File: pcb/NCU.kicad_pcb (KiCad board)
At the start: 4 copper layers, 100 x 150 mm, 332 parts, among them IC1 VND7E025AJTR, IC2 ESP32-C6-WROOM-1-N8, IC3 ESD2CAN24DBZRQ1, IC4 VND7E025AJTR, IC5 ESD2CAN24DBZRQ1, IC6 LMR51460SQDRRRQ1, IC7 TPS628101HQWRWYRQ1, IC8 LP2951-50DRG4, IC9 TPS2121RUXT, J1 6437288-4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

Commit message: initial microcontroller layout
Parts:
- JP6, JP7, JP8: moved to B.Cu
- L1: value VLS3015CX-2R2M-H -> 2.2uH; footprint SamacSys_Parts:VLS3015 -> Inductor_SMD:L_0805_2012Metric_Pad1.05x1.20mm_HandSolder
- moved D27 322.6 mm to (145.4, 127.0)
- moved D26 322.2 mm to (140.7, 155.9)
- moved U7 313.1 mm to (130.9, 137.3)
- moved TP18 313.1 mm to (125.6, 116.9), turned to 90 degrees
- moved R124 311.5 mm to (140.7, 154.4)
- moved JP12 296.9 mm to (125.0, 119.8), turned to 180 degrees
- moved TP19 295.8 mm to (105.7, 141.3)
- moved Y2 292.7 mm to (108.5, 133.3), turned to 90 degrees
- moved R125 289.5 mm to (125.0, 121.8), turned to 180 degrees
- moved Y3 287.7 mm to (112.4, 146.6)
- moved C90 284.7 mm to (112.3, 144.4), turned to 180 degrees
- moved C92 284.6 mm to (112.3, 149.2)
- moved R126 284.3 mm to (120.1, 121.8)
- moved C89 281.6 mm to (109.6, 140.4), turned to 90 degrees
- moved C17 279.7 mm to (147.1, 134.6), turned to 90 degrees
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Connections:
- C91 pad 1: /MCU/RCC_OSC_OUT -> /MCU/RCC_OSC32_OUT
- C93 pad 1: /MCU/RCC_OSC_IN -> /MCU/RCC_OSC32_IN
- Y2 pad 1: /MCU/RCC_OSC_OUT -> /MCU/RCC_OSC32_OUT
- Y2 pad 2: /MCU/RCC_OSC_IN -> /MCU/RCC_OSC32_IN
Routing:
- net 3V3: track 10.4 -> 130.9 mm, vias 10 -> 30
- net /MCU/MCU Power/VDDLDO: track 0.00 -> 77.3 mm, vias 0 -> 3
- net /MCU/VCAP: track 0.00 -> 73.0 mm, vias 0 -> 3
- net GND: track 14.0 -> 77.3 mm, vias 53 -> 101
- net /MCU/RCC_OSC_IN: track 0.00 -> 20.4 mm
- net /MCU/STM_NRST: track 0.00 -> 15.7 mm, vias 0 -> 2
- net /MCU/MCU Power/1V2_MCU: track 0.00 -> 14.9 mm, vias 0 -> 1
- net /MCU/RCC_OSC32_OUT: track 0.00 -> 14.5 mm
- net /MCU/RCC_OSC32_IN: track 0.00 -> 14.4 mm
- net Net-(JP12-A): track 0.00 -> 11.1 mm
- net /MCU/RCC_OSC_OUT: track 0.00 -> 11.1 mm
- net Net-(U7-PE15): track 0.00 -> 8.41 mm
- net /MCU/MCU Power/VDDA: track 0.00 -> 8.27 mm, vias 0 -> 1
- net /MCU/VREF+: track 0.00 -> 7.61 mm, vias 0 -> 1
- net /MCU/VFBSMPS: track 0.00 -> 7.45 mm, vias 0 -> 1
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- added copper zone on In2.Cu, net 3V3

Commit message: laid out analogs
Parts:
- JP11: moved to B.Cu
- moved TP14 356.3 mm to (181.8, 96.6), turned to 90 degrees
- moved TP15 356.1 mm to (181.8, 103.6), turned to 90 degrees
- moved R85 350.3 mm to (183.5, 100.1), turned to -90 degrees
- moved IC3 347.0 mm to (180.7, 100.1), turned to 180 degrees
- moved U4 343.1 mm to (174.9, 100.0)
- moved C67 341.2 mm to (170.4, 100.1), turned to 90 degrees
- moved C66 339.5 mm to (168.8, 100.1), turned to 90 degrees
- moved TP17 330.7 mm to (181.7, 91.7), turned to 90 degrees
- moved TP16 330.2 mm to (181.7, 84.7), turned to 90 degrees
- moved R109 323.0 mm to (183.5, 88.2), turned to -90 degrees
- moved IC5 320.4 mm to (180.7, 88.2), turned to 180 degrees
- moved U5 317.6 mm to (174.9, 88.2)
- moved C72 314.3 mm to (170.3, 88.0), turned to 90 degrees
- moved C71 313.0 mm to (168.7, 88.0), turned to 90 degrees
- moved D10 257.5 mm to (86.7, 124.2)
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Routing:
- net AGND: track 17.7 -> 73.9 mm, vias 5 -> 40
- net 3V3: track 130.9 -> 157.9 mm, vias 30 -> 45
- net GND: track 77.3 -> 90.0 mm, vias 101 -> 111
- net /CONN_A/CAN0_L: track 0.00 -> 8.83 mm
- net /CONN_A/CAN0_H: track 0.00 -> 8.80 mm
- net /CONN_A/CAN1_L: track 0.00 -> 8.79 mm
- net /CONN_A/CAN1_H: track 0.00 -> 8.75 mm
- net /INPUTS/DIN2_IO: track 0.00 -> 3.74 mm
- net /GPIO/GPIO1_IO: track 0.00 -> 3.73 mm
- net /GPIO/GPIO2_IO: track 0.00 -> 3.72 mm
- net /GPIO/GPIO3_IO: track 0.00 -> 3.72 mm
- net /INPUTS/AIN0_IO: track 0.00 -> 3.71 mm
- net /INPUTS/AIN2_IO: track 0.00 -> 3.71 mm
- net /INPUTS/12V_IO: track 0.00 -> 3.70 mm
- net /INPUTS/DIN1_IO: track 0.00 -> 3.70 mm
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
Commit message: v2 analogs routing
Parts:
- moved D14 343.8 mm to (145.8, 114.8), turned to 180 degrees
- moved R49 340.6 mm to (143.2, 111.9), turned to 0 degrees
- moved C50 339.8 mm to (143.2, 113.4), turned to 180 degrees
- moved D6 334.9 mm to (145.9, 119.3), turned to 180 degrees
- moved D18 334.6 mm to (135.0, 113.8), turned to 180 degrees
- moved R47 334.2 mm to (139.9, 111.9), turned to 0 degrees
- moved R48 333.3 mm to (139.8, 113.4), turned to 180 degrees
- moved R19 331.5 mm to (143.2, 116.4), turned to 0 degrees
- moved R67 331.5 mm to (132.3, 110.9), turned to 0 degrees
- moved C12 330.8 mm to (143.2, 117.9), turned to 180 degrees
- moved C56 330.6 mm to (132.3, 112.4), turned to 180 degrees
- moved D11 325.9 mm to (145.8, 123.9), turned to 180 degrees
- moved D16 325.5 mm to (135.0, 118.3), turned to 180 degrees
- moved R63 325.3 mm to (129.0, 110.9), turned to 0 degrees
- moved R17 325.2 mm to (139.9, 116.4), turned to 0 degrees
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
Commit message: routed LSDs
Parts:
- moved R86 356.1 mm to (212.4, 135.3), turned to 180 degrees
- moved R87 355.8 mm to (212.4, 136.9), turned to 180 degrees
- moved S2 355.2 mm to (217.9, 137.2)
- moved R89 354.9 mm to (212.4, 138.5)
- moved R20 354.6 mm to (212.4, 141.7), turned to 180 degrees
- moved R21 354.3 mm to (212.4, 143.3), turned to 180 degrees
- moved R88 354.3 mm to (212.4, 133.7), turned to 180 degrees
- moved S1 353.7 mm to (217.9, 143.7)
- moved R23 353.5 mm to (212.4, 144.9)
- moved R22 352.9 mm to (212.4, 140.1), turned to 180 degrees
- moved R104 347.7 mm to (212.4, 154.5), turned to 180 degrees
- moved R105 347.4 mm to (212.4, 156.1), turned to 180 degrees
- moved S4 346.8 mm to (217.9, 156.4)
- moved R107 346.3 mm to (212.4, 157.7)
- moved R106 345.6 mm to (212.4, 152.9), turned to 180 degrees
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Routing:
- net 3V3: track 157.9 -> 215.0 mm, vias 45 -> 49
- net /MCU/MCU Power/VDDLDO: track 77.3 -> 24.4 mm
- net GND: track 90.0 -> 94.3 mm, vias 111 -> 139
- net Net-(S2-STATUS): track 0.00 -> 4.24 mm
- net Net-(S1-STATUS): track 0.00 -> 4.23 mm
- net Net-(S3-STATUS): track 0.00 -> 4.17 mm
- net Net-(S4-STATUS): track 0.00 -> 4.16 mm
- net Net-(S1-IN): track 0.00 -> 3.51 mm
- net Net-(S2-IN): track 0.00 -> 3.49 mm
- net Net-(S3-IN): track 0.00 -> 3.49 mm
- net Net-(S4-IN): track 0.00 -> 3.48 mm

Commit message: initial hsd layout
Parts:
- D23, D7: value 1N4148 -> 1N4148W; footprint Diode_THT:D_DO-35_SOD27_P7.62mm_Horizontal -> Diode_SMD:D_SOD-123
- moved R104 126.0 mm to (93.2, 113.6)
- moved R106 126.0 mm to (93.2, 112.0)
- moved R21 126.0 mm to (93.2, 102.4)
- moved R23 126.0 mm to (93.2, 104.0)
- moved R86 126.0 mm to (93.2, 94.4)
- moved R89 126.0 mm to (93.2, 97.6)
- moved R92 126.0 mm to (93.2, 105.6)
- moved S1 126.0 mm to (98.7, 102.8)
- moved S2 126.0 mm to (98.7, 96.3)
- moved S4 126.0 mm to (98.7, 115.5)
- moved R87 126.0 mm to (93.2, 96.0)
- moved R93 126.0 mm to (93.2, 110.4)
- moved R105 126.0 mm to (93.2, 115.2)
- moved R107 126.0 mm to (93.2, 116.8)
- moved R22 126.0 mm to (93.2, 99.2)
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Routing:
- net GND: track 94.3 -> 108.2 mm, vias 139 -> 153
- net Net-(IC4-~{FAULTRST}): track 0.00 -> 8.07 mm
- net Net-(IC1-~{FAULTRST}): track 0.00 -> 7.88 mm
- net Net-(IC1-CS): track 0.00 -> 7.40 mm
- net Net-(IC4-CS): track 0.00 -> 7.40 mm
- net Net-(IC4-SEN): track 0.00 -> 7.07 mm
- net Net-(D7-A): track 0.00 -> 6.91 mm
- net Net-(D23-A): track 0.00 -> 6.89 mm
- net Net-(IC1-SEN): track 0.00 -> 6.88 mm
- net Net-(IC1-SEL0): track 0.00 -> 5.69 mm
- net Net-(IC4-SEL0): track 0.00 -> 5.68 mm
- net Net-(IC1-INPUT0): track 0.00 -> 3.37 mm
- net Net-(IC4-INPUT0): track 0.00 -> 3.33 mm
- net Net-(IC4-INPUT1): track 0.00 -> 3.33 mm
- net Net-(IC1-INPUT1): track 0.00 -> 3.31 mm
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- added copper zone on F.Cu, net /CONN_A/HSD_0
- added copper zone on F.Cu, net /CONN_A/HSD_1
- added copper zone on F.Cu, net /CONN_A/HSD_2
- added copper zone on F.Cu, net /CONN_A/HSD_3

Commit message: improved power supplies I think
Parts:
- moved D14 294.5 mm to (-14.6, -31.6), turned to -90 degrees
- moved D6 293.0 mm to (-10.1, -31.6), turned to -90 degrees
- moved R49 292.0 mm to (-17.5, -28.9), turned to 90 degrees
- moved D11 291.5 mm to (-5.52, -31.6), turned to -90 degrees
- moved C50 291.4 mm to (-16.0, -28.9), turned to -90 degrees
- moved R19 290.3 mm to (-13.0, -28.9), turned to 90 degrees
- moved D15 290.2 mm to (-1.07, -31.6), turned to -90 degrees
- moved C12 289.8 mm to (-11.5, -28.9), turned to -90 degrees
- moved R42 288.8 mm to (-8.47, -28.9), turned to 90 degrees
- moved C48 288.3 mm to (-6.97, -28.9), turned to -90 degrees
- moved R47 287.5 mm to (-17.5, -25.6), turned to 90 degrees
- moved R52 287.4 mm to (-3.97, -29.0), turned to 90 degrees
- moved C51 286.9 mm to (-2.47, -29.0), turned to -90 degrees
- moved R48 286.8 mm to (-16.0, -25.6), turned to -90 degrees
- moved R17 285.8 mm to (-13.0, -25.6), turned to 90 degrees
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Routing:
- net Net-(IC9-CP2): track 5.80 -> 14.2 mm
- net Net-(IC9-PR1): track 4.45 -> 10.1 mm
- net GND: track 108.2 -> 107.2 mm, vias 153 -> 156
- net 5V: vias 3 -> 21

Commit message: improved power input stage, possible drive placement
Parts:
- moved C81 192.4 mm to (-13.8, 57.3)
- moved IC7 192.4 mm to (-13.8, 60.4)
- moved R114 192.4 mm to (-17.3, 61.3)
- moved TP9 192.4 mm to (-18.5, 68.9)
- moved C80 192.4 mm to (-9.38, 60.6)
- moved C82 192.4 mm to (-9.38, 63.8)
- moved C83 192.4 mm to (-14.5, 68.7)
- moved C84 192.4 mm to (-14.5, 71.2)
- moved C85 192.4 mm to (-14.5, 73.2)
- moved C86 192.4 mm to (-7.60, 25.9)
- moved C87 192.4 mm to (-17.7, 27.9)
- moved IC8 192.4 mm to (-13.1, 27.9)
- moved L3 192.4 mm to (-15.0, 65.3)
- moved R115 192.4 mm to (-9.38, 59.0)
- moved R116 192.4 mm to (-9.38, 65.4)
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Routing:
- net LV_5V: vias 15 -> 30
- net 12V: vias 0 -> 24
- net /PWR/PWR_LV_5V/LMR_SW: vias 0 -> 8

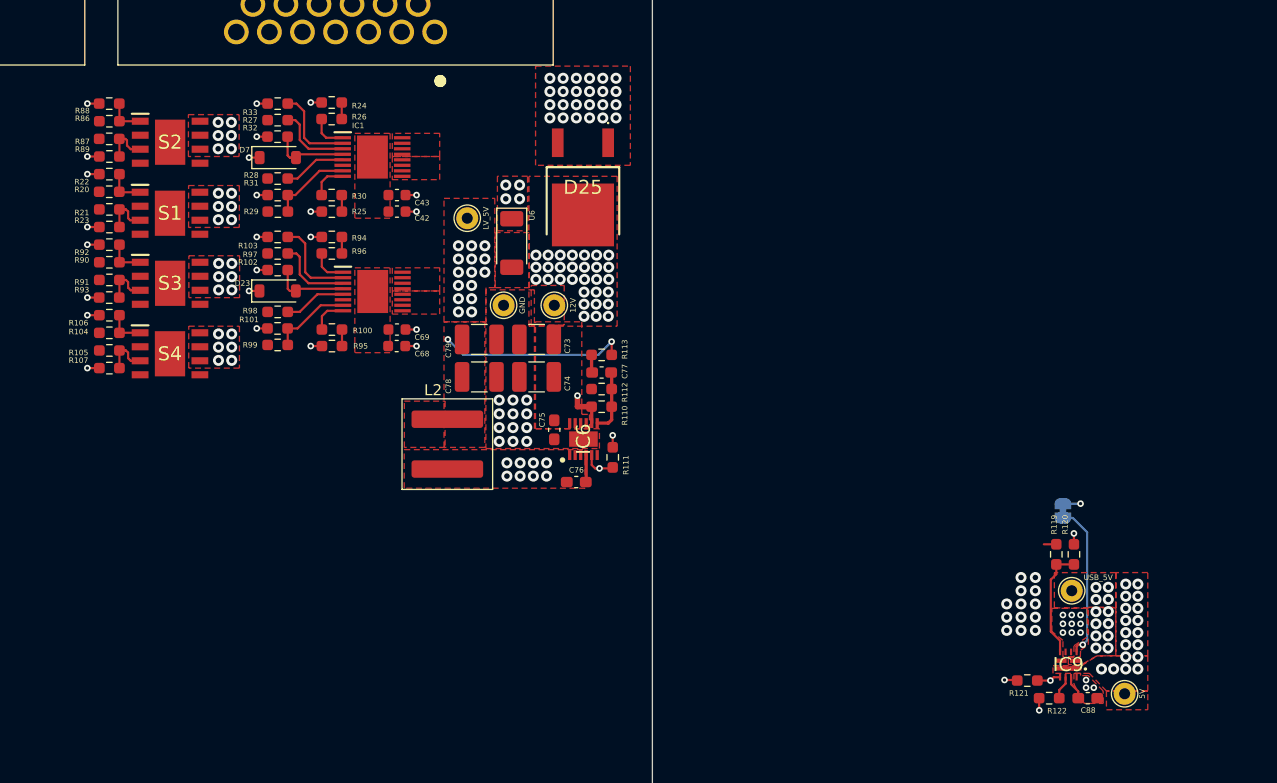
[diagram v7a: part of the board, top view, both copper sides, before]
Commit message: better power mux layout
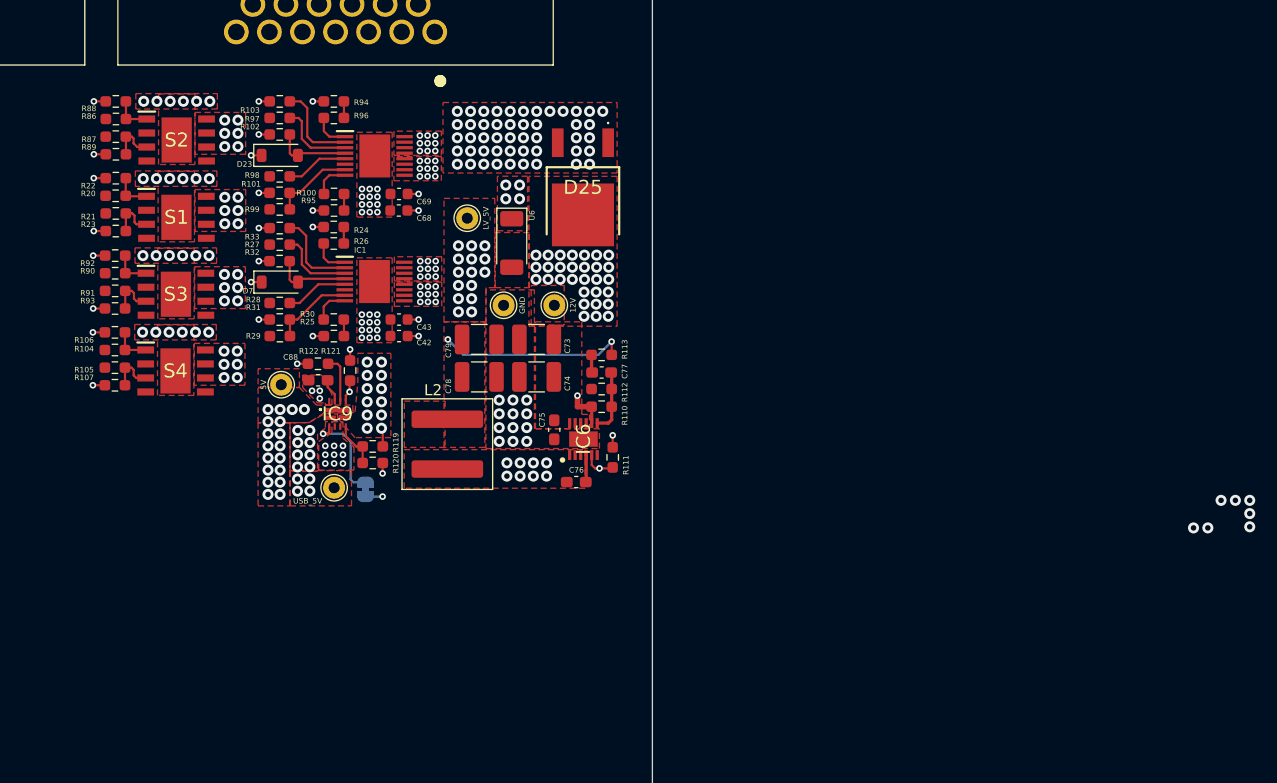
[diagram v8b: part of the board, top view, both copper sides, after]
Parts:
- moved TP8 81.5 mm to (116.3, 101.0), turned to 0 degrees
- moved C88 75.6 mm to (119.7, 100.6), turned to 180 degrees
- moved R122 73.0 mm to (119.7, 99.1)
- moved IC9 70.1 mm to (121.4, 103.7), turned to 0 degrees
- moved R121 67.6 mm to (122.6, 99.7), turned to -90 degrees
- moved TP6 67.6 mm to (121.1, 110.4), turned to -90 degrees
- moved R120 64.2 mm to (124.6, 108.1), turned to 0 degrees
- moved JP11 63.3 mm to (124.0, 110.5), turned to -90 degrees
- moved R119 62.8 mm to (124.6, 106.6), turned to 180 degrees
- moved R101 12.3 mm to (116.2, 83.6)
- moved R98 12.3 mm to (116.2, 82.1)
- moved R99 12.3 mm to (116.2, 85.1)
- moved C68 12.3 mm to (127.0, 85.2)
- moved C69 12.3 mm to (127.0, 83.7)
- moved D23 12.3 mm to (116.2, 80.2)
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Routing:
- net 3V3: track 217.0 -> 164.0 mm
- net USB_VBUS: track 0.00 -> 52.8 mm
- net 5V: track 11.0 -> 56.2 mm
- net /MCU/VCAP: track 73.0 -> 27.8 mm
- net Net-(IC9-PR1): track 10.1 -> 4.28 mm
- net Net-(IC9-CP2): track 14.2 -> 8.81 mm
- net Net-(IC9-ILIM): track 2.14 -> 4.36 mm
- net LV_5V: track 19.1 -> 19.6 mm, vias 30 -> 36
- net 12V_PRT: vias 31 -> 55
- net 12V: vias 24 -> 48
- net /CONN_A/LSD_3: vias 0 -> 6
- net /CONN_A/LSD_2: vias 0 -> 6
- net /CONN_A/LSD_1: vias 0 -> 6
- net /CONN_A/LSD_0: vias 0 -> 6
- net /CONN_A/HSD_3: vias 0 -> 9
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- added copper zone on F.Cu, net /CONN_A/LSD_0
- added copper zone on F.Cu, net /CONN_A/LSD_1
- added copper zone on F.Cu, net /CONN_A/LSD_2
- added copper zone on F.Cu, net /CONN_A/LSD_3
